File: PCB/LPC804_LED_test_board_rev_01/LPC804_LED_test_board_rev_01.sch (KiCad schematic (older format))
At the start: 16 parts

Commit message: Generated Netlist
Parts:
- added Q?: PN2222A, Package_TO_SOT_THT:TO-92_Inline, symbol Transistor_BJT:PN2222A
- added RN?: R_Pack04, symbol Device:R_Pack04
- BT1, BT2, BT3: renamed from BT?; footprint (none) -> Battery:BatteryHolder_Keystone_1060_1x2032
- C1, C2, C3, C4, C5, C6: renamed from C?; footprint (none) -> Capacitor_SMD:C_0805_2012Metric
- J1: renamed from J?; footprint (none) -> Connector_PinHeader_1.27mm:PinHeader_2x05_P1.27mm_Vertical
- U3: renamed from U?; footprint (none) -> Package_SO:TSSOP-24_4.4x7.8mm_P0.65mm
- gave numbers to parts that had none: 5
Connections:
- net 6v: now also RN?.8 (R1.2)
- net GND: now also Q?.1 (E)
- net WS_Data renamed R1
- net R1: now also Q?.3 (C), RN?.1 (R1.1); no longer U3.1 (PIO0_18)
- new net: RN?.2 (R2.1), RN?.3 (R3.1)
- new net: RN?.5 (R4.2), RN?.6 (R3.2)
- new net WS_Data_MCU: RN?.7 (R2.2), U3.1 (PIO0_18)
- new net trig: Q?.2 (B), RN?.4 (R4.1)

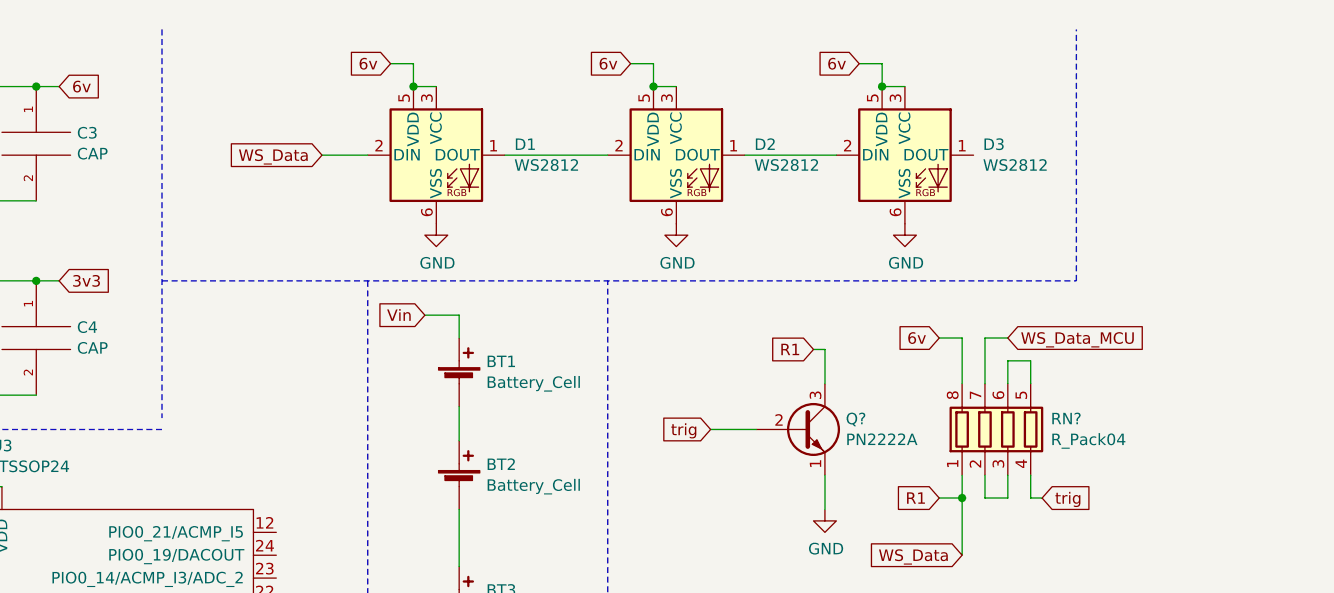
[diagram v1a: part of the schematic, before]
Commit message: Added 4th WS2812
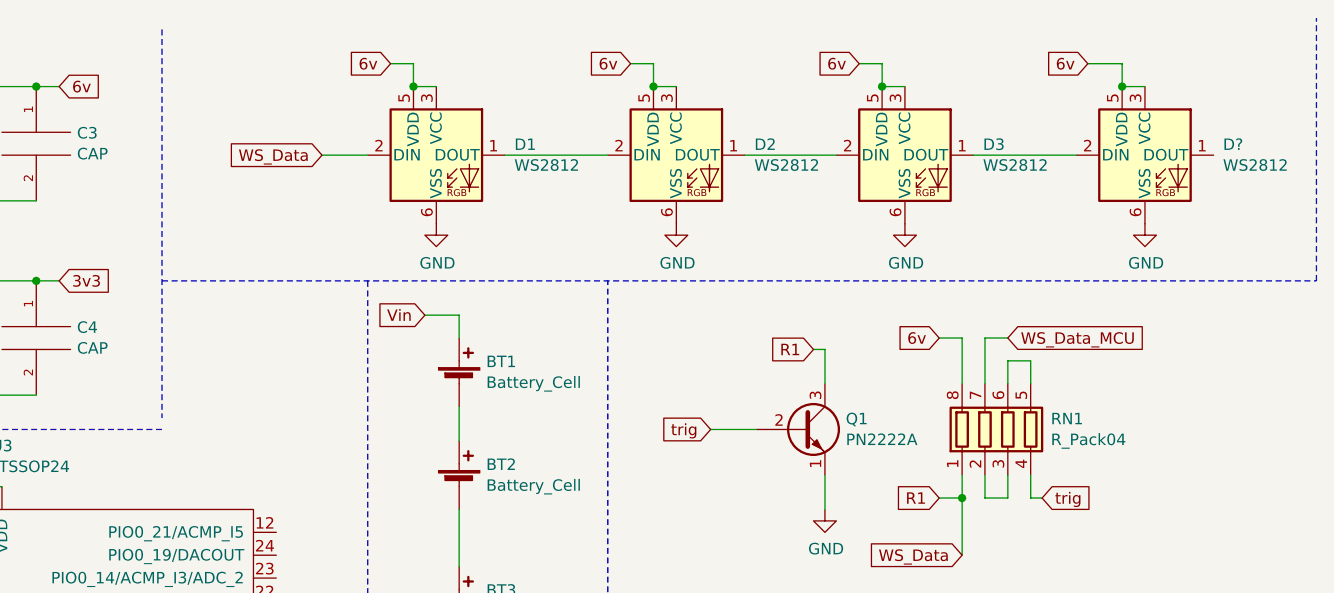
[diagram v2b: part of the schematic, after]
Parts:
- added D?: WS2812, LED_SMD:LED_WS2812_PLCC6_5.0x5.0mm_P1.6mm, symbol LED:WS2812
- RN1: renamed from RN?; footprint (none) -> Resistor_SMD:R_Array_Convex_4x0603
- gave numbers to parts that had none: 1
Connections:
- net 6v: now also D?.3 (VCC), D?.5 (VDD)
- net GND: now also D?.6 (VSS)
- net at D3.1 (DOUT): now also D?.2 (DIN)
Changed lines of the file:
@@
 Wire Wire Line
 	3600 1050 3800 1050
-Wire Notes Line
-	2900 1600 6900 1600
-Wire Notes Line
-	6900 1600 6900 500
 Text GLabel 1050 2400 0    50   Input ~ 0
 WS_Data_MCU
@@
 	4850 3550 4850 1600
 $Comp
-L Transistor_BJT:PN2222A Q?
+L Transistor_BJT:PN2222A Q1
 U 1 1 5DB9156E
 P 5700 2250
-F 0 "Q?" H 5891 2296 50  0000 L CNN
+F 0 "Q1" H 5891 2296 50  0000 L CNN
 F 1 "PN2222A" H 5891 2205 50  0000 L CNN
 F 2 "Package_TO_SOT_THT:TO-92_Inline" H 5900 2175 50  0001 L CIN
@@
 $EndComp
 $Comp
-L Device:R_Pack04 RN?
+L Device:R_Pack04 RN1
 U 1 1 5DB91ECF
 P 6600 2250
-F 0 "RN?" H 6788 2296 50  0000 L CNN
+F 0 "RN1" H 6788 2296 50  0000 L CNN
 F 1 "R_Pack04" H 6788 2205 50  0000 L CNN
-F 2 "" V 6875 2250 50  0001 C CNN
+F 2 "Resistor_SMD:R_Array_Convex_4x0603" V 6875 2250 50  0001 C CNN
 F 3 "~" H 6600 2250 50  0001 C CNN
 	1    6600 2250
@@
 $EndComp
 $Comp
-L power:GND #PWR?
+L power:GND #PWR010
 U 1 1 5DB920B1
 P 5800 2600
-F 0 "#PWR?" H 5800 2350 50  0001 C CNN
+F 0 "#PWR010" H 5800 2350 50  0001 C CNN
 F 1 "GND" H 5805 2427 50  0000 C CNN
 F 2 "" H 5800 2600 50  0001 C CNN
@@
 	6400 2550 6400 2800
 Connection ~ 6400 2550
+$Comp
+L LED:WS2812 D?
+U 1 1 5DBA6030
+P 7200 1050
+F 0 "D?" H 7541 1096 50  0000 L CNN
+F 1 "WS2812" H 7541 1005 50  0000 L CNN
+F 2 "LED_SMD:LED_WS2812_PLCC6_5.0x5.0mm_P1.6mm" H 7250 750 50  0001 L TNN
+F 3 "https://cdn-shop.adafruit.com/datasheets/WS2812.pdf" H 7300 675 50  0001 L TNN
+	1    7200 1050
+	1    0    0    -1
+$EndComp
+Wire Wire Line
+	6450 1050 6900 1050
+$Comp
+L power:GND #PWR?
+U 1 1 5DBA7E79
+P 7200 1350
+F 0 "#PWR?" H 7200 1100 50  0001 C CNN
+F 1 "GND" H 7205 1177 50  0000 C CNN
+F 2 "" H 7200 1350 50  0001 C CNN
+F 3 "" H 7200 1350 50  0001 C CNN
+	1    7200 1350
+	1    0    0    -1
+$EndComp
+Text GLabel 6950 650  0    50   Input ~ 0
+6v
+Wire Wire Line
+	6950 650  7100 650
+Wire Wire Line
+	7100 650  7100 750
+Wire Wire Line
+	7100 750  7200 750
+Connection ~ 7100 750
+Wire Notes Line
+	7950 1600 7950 450
+Wire Notes Line
+	2900 1600 7950 1600
 $EndSCHEMATC
